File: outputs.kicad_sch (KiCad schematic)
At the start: 42 parts, among them Q1 SQ2362CES, Q3 SQ2362CES, Q6 SQ2362CES, Q7 SQ2362CES, Q8 SQ2362CES, U2 LM393

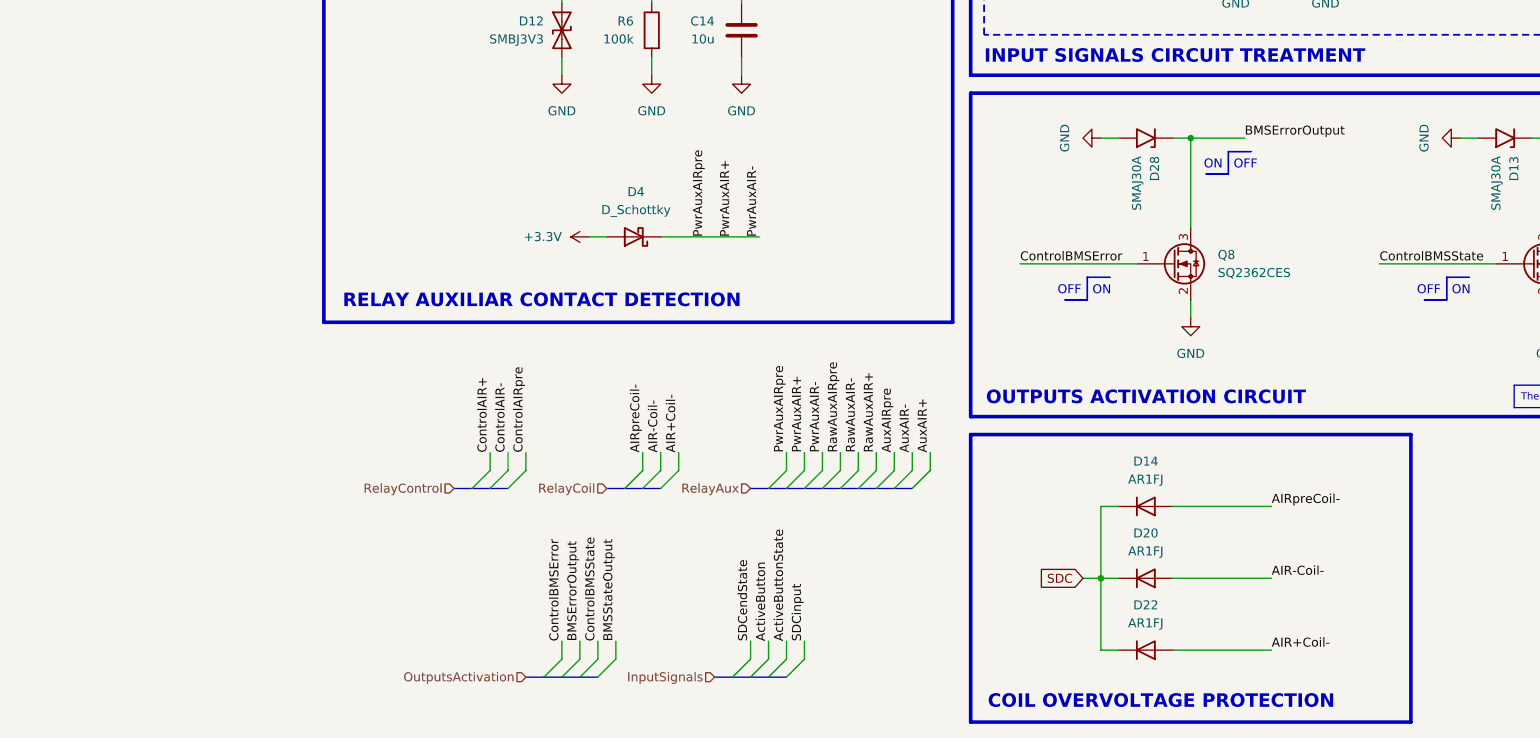
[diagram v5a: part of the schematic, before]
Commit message: - S'han afegit uns connectors preliminar \n-S'han eliminat els diodes de protecció dels airs
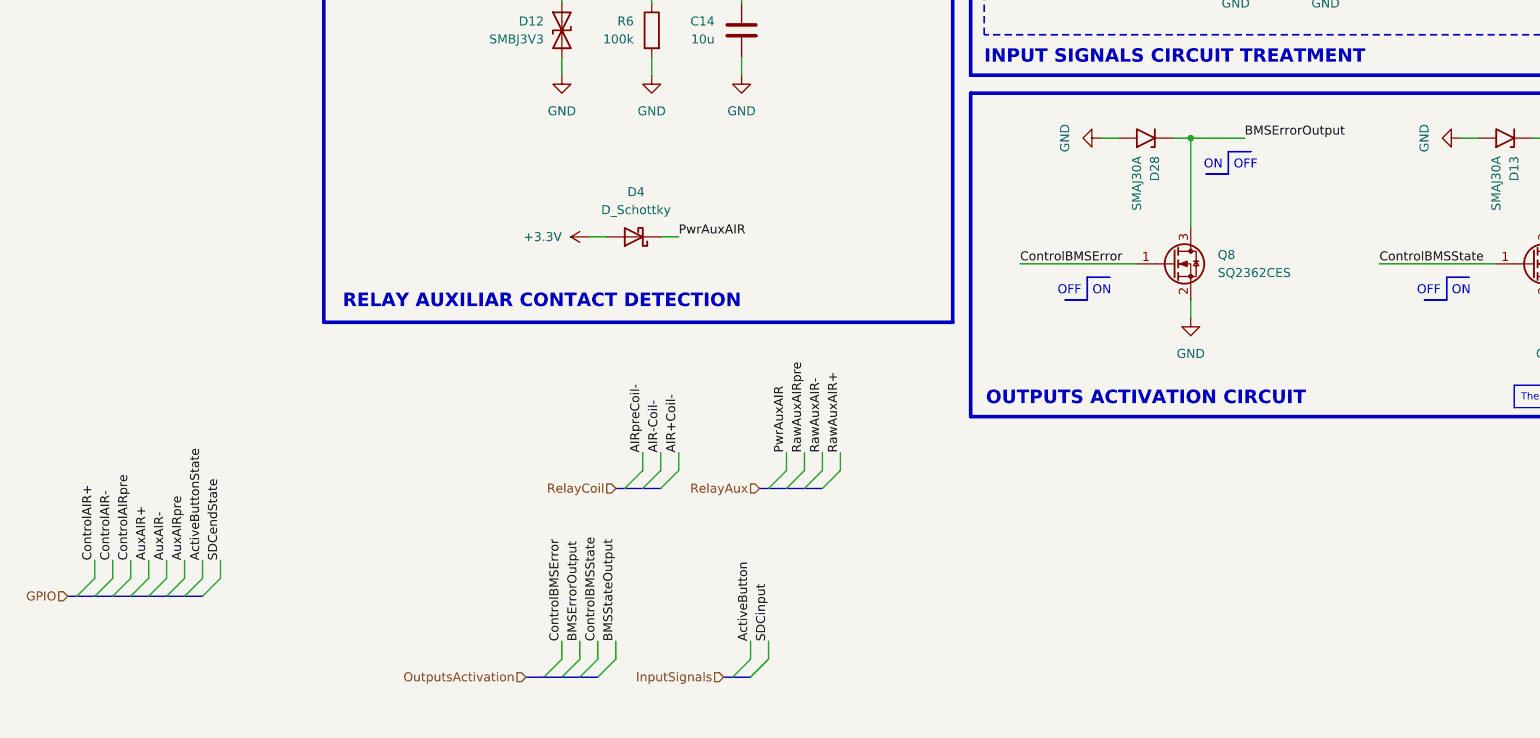
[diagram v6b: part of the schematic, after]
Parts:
- removed D14, D20, D22: AR1FJ, Diode_SMD:D_SMF, symbol Device:D
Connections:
- net PwrAuxAIR+ renamed PwrAuxAIR
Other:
- note removed: "COIL OVERVOLTAGE PROTECTION"

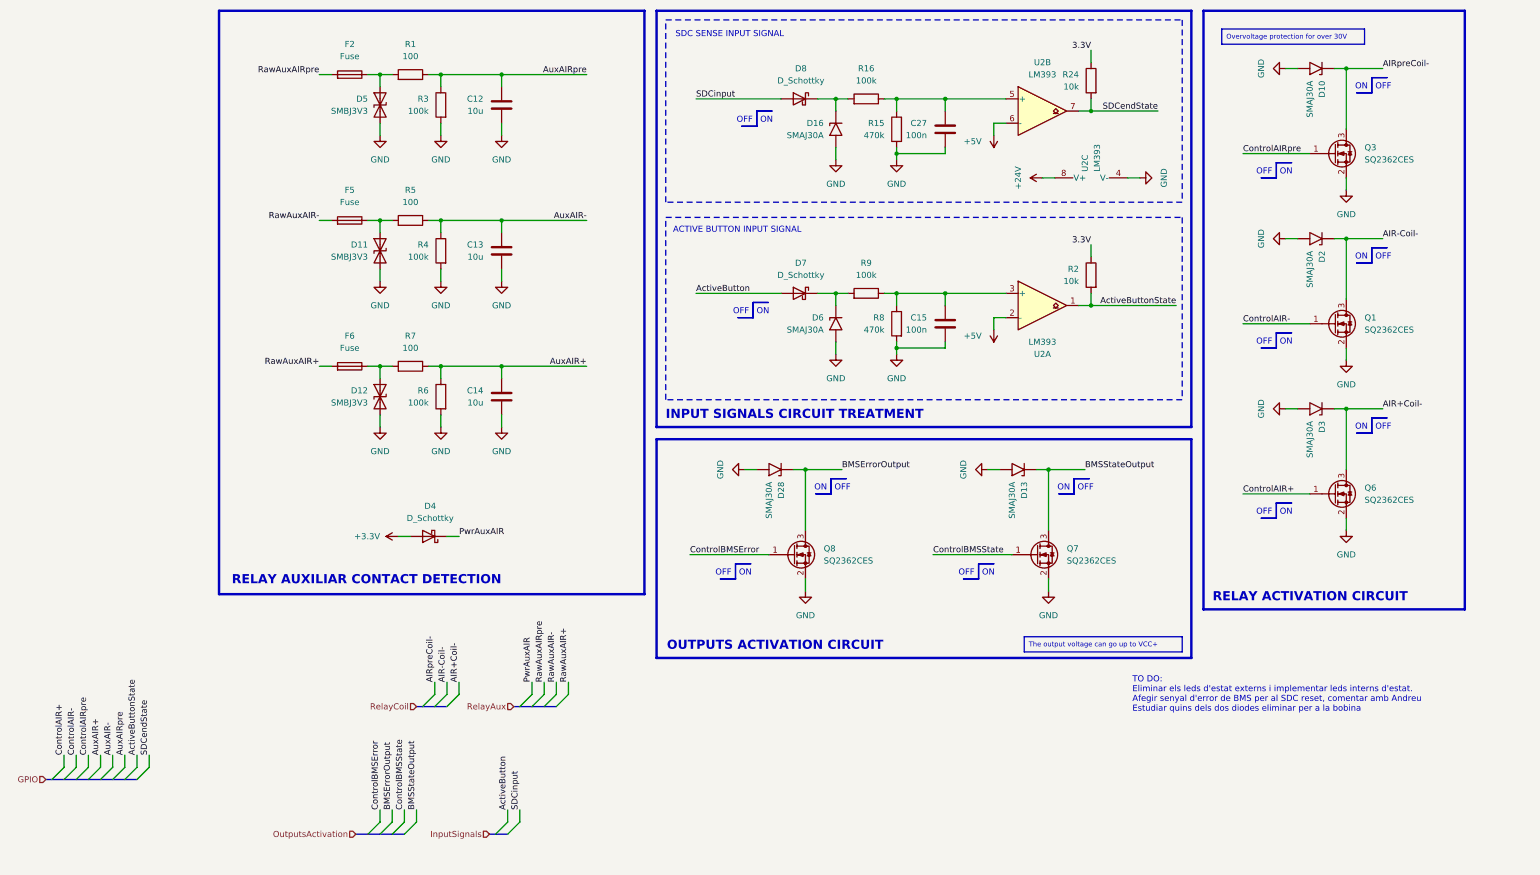
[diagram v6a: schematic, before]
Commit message: Modificació de les etiquetes a globals Filtre afegit al transformador de isoSPI Leds indicadors per estat i error Senyal d'error de BMS per el sdcreset
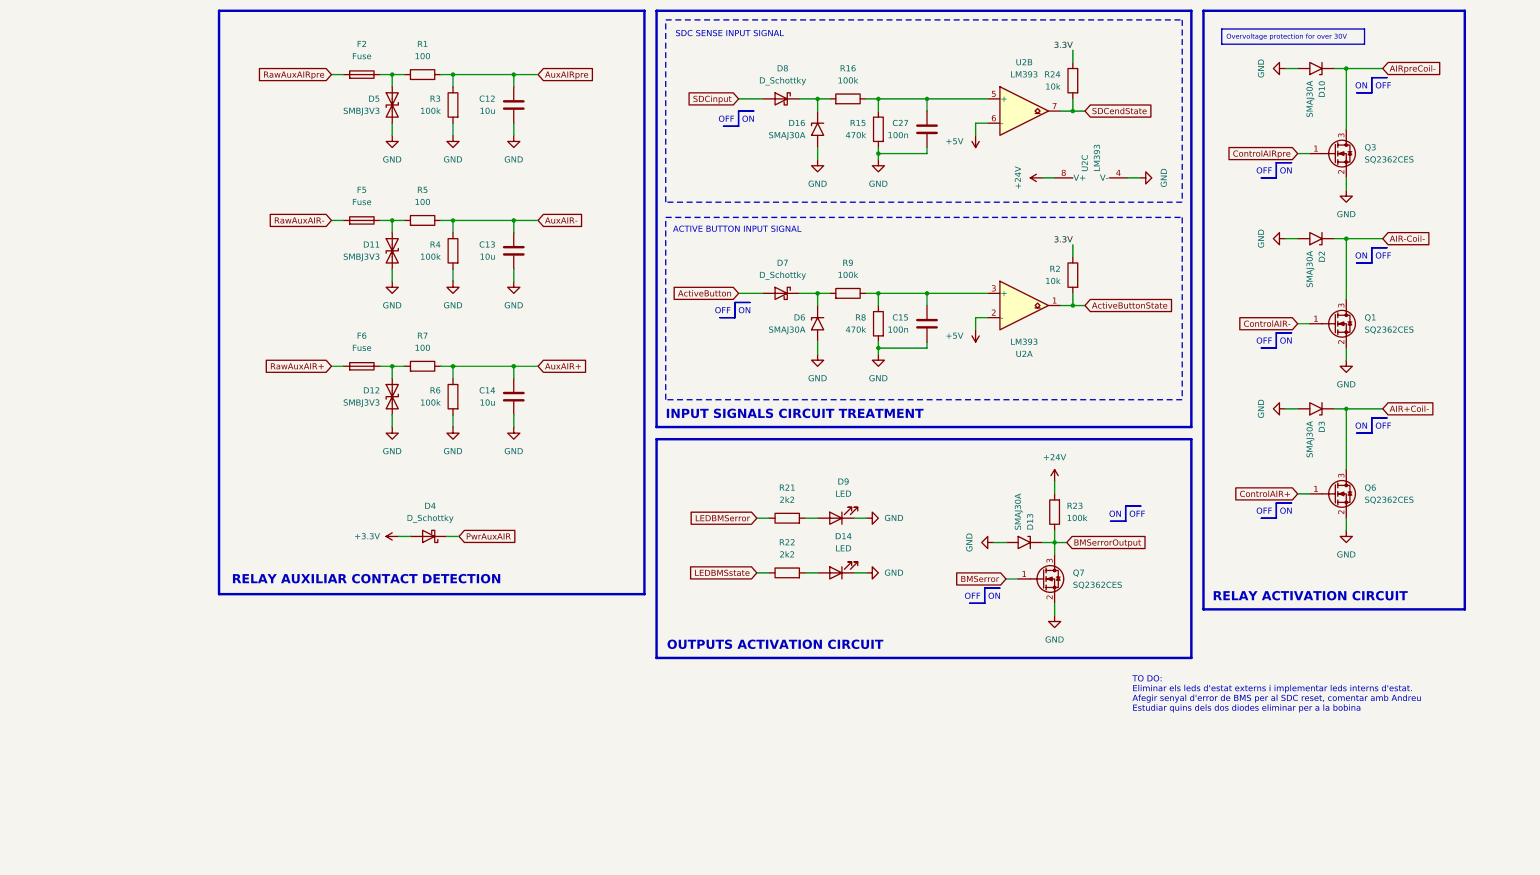
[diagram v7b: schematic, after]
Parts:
- removed D28: SMAJ30A, Diode_SMD:D_SMA, symbol Diode:SMAJ30A
- removed Q8: SQ2362CES, Package_TO_SOT_SMD:SOT-23, symbol Transistor_FET:2N7002
- added D14, D9: LED, LED_SMD:LED_0603_1608Metric_Pad1.05x0.95mm_HandSolder, symbol Device:LED
- added R21, R22: 2k2, Resistor_SMD:R_0603_1608Metric, symbol Device:R
- added R23: 100k, Resistor_SMD:R_0603_1608Metric, symbol Device:R
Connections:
- net +24V: now also R23.2
- net GND: now also D14.1 (K), D9.1 (K)
- net BMSStateOutput renamed BMSerrorOutput
- net BMSerrorOutput: now also R23.1
- net ControlBMSState renamed BMSerror
- new net: D14.2 (A), R22.2
- new net: D9.2 (A), R21.2
- new net LEDBMSerror: R21.1
- new net LEDBMSstate: R22.1
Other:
- moved on the sheet: C12, C13, C14, C15, C27, D11, D12, D13, D16, D5, D6, D7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

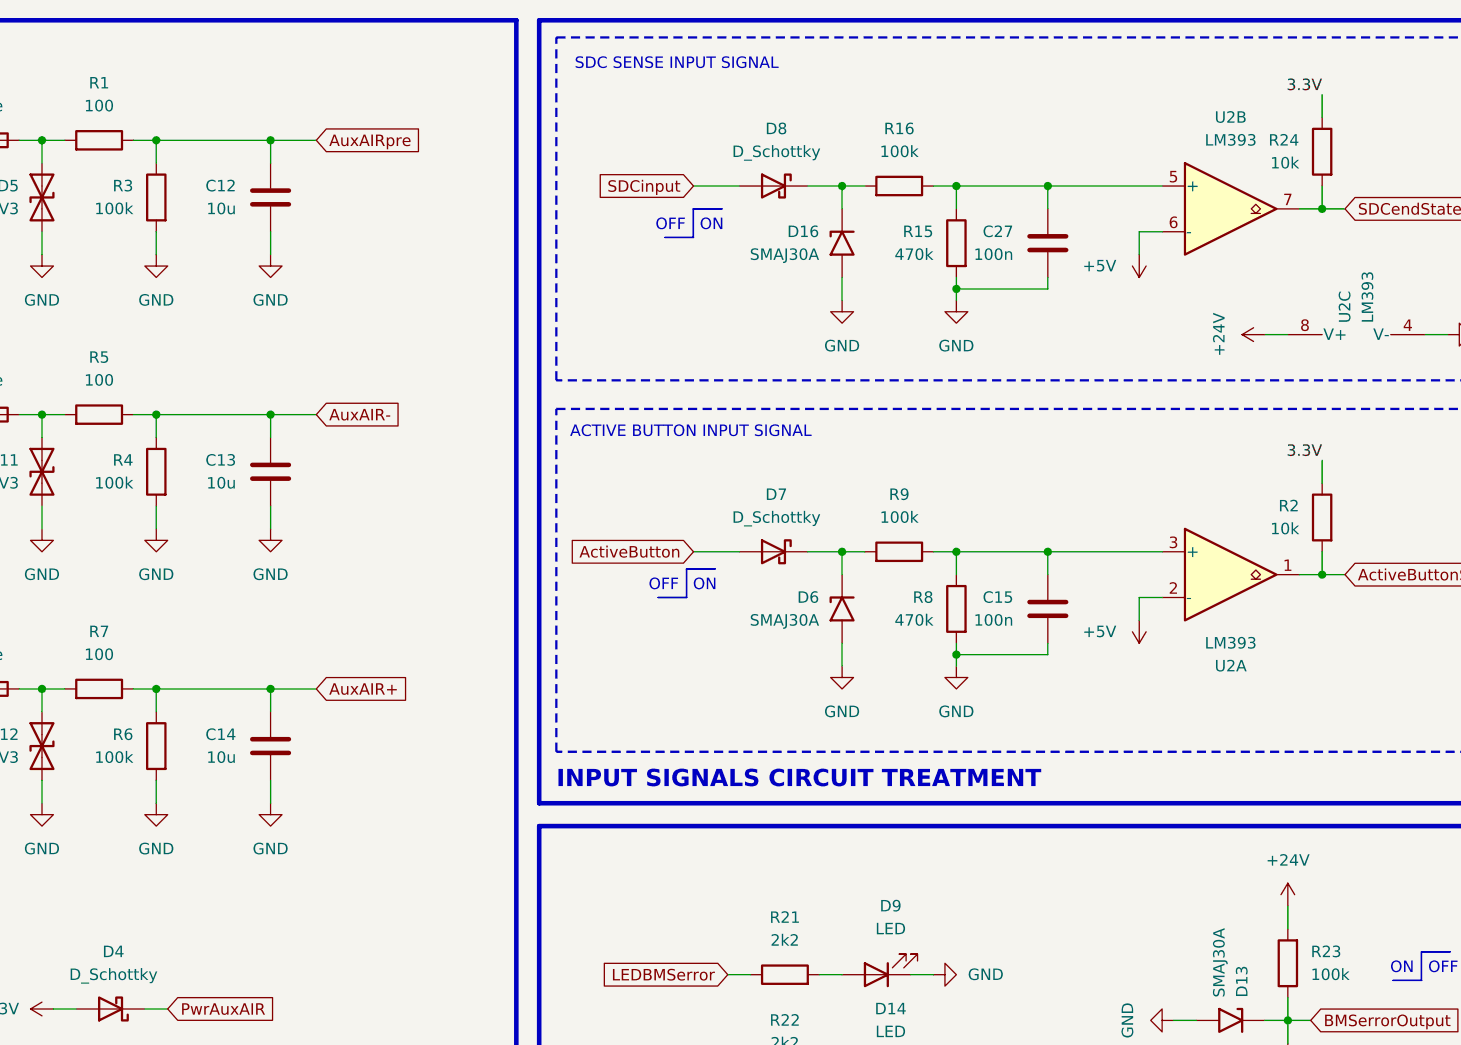
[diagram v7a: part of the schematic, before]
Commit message: Revisió dels valors de filtres, divisors de tensió i resistències
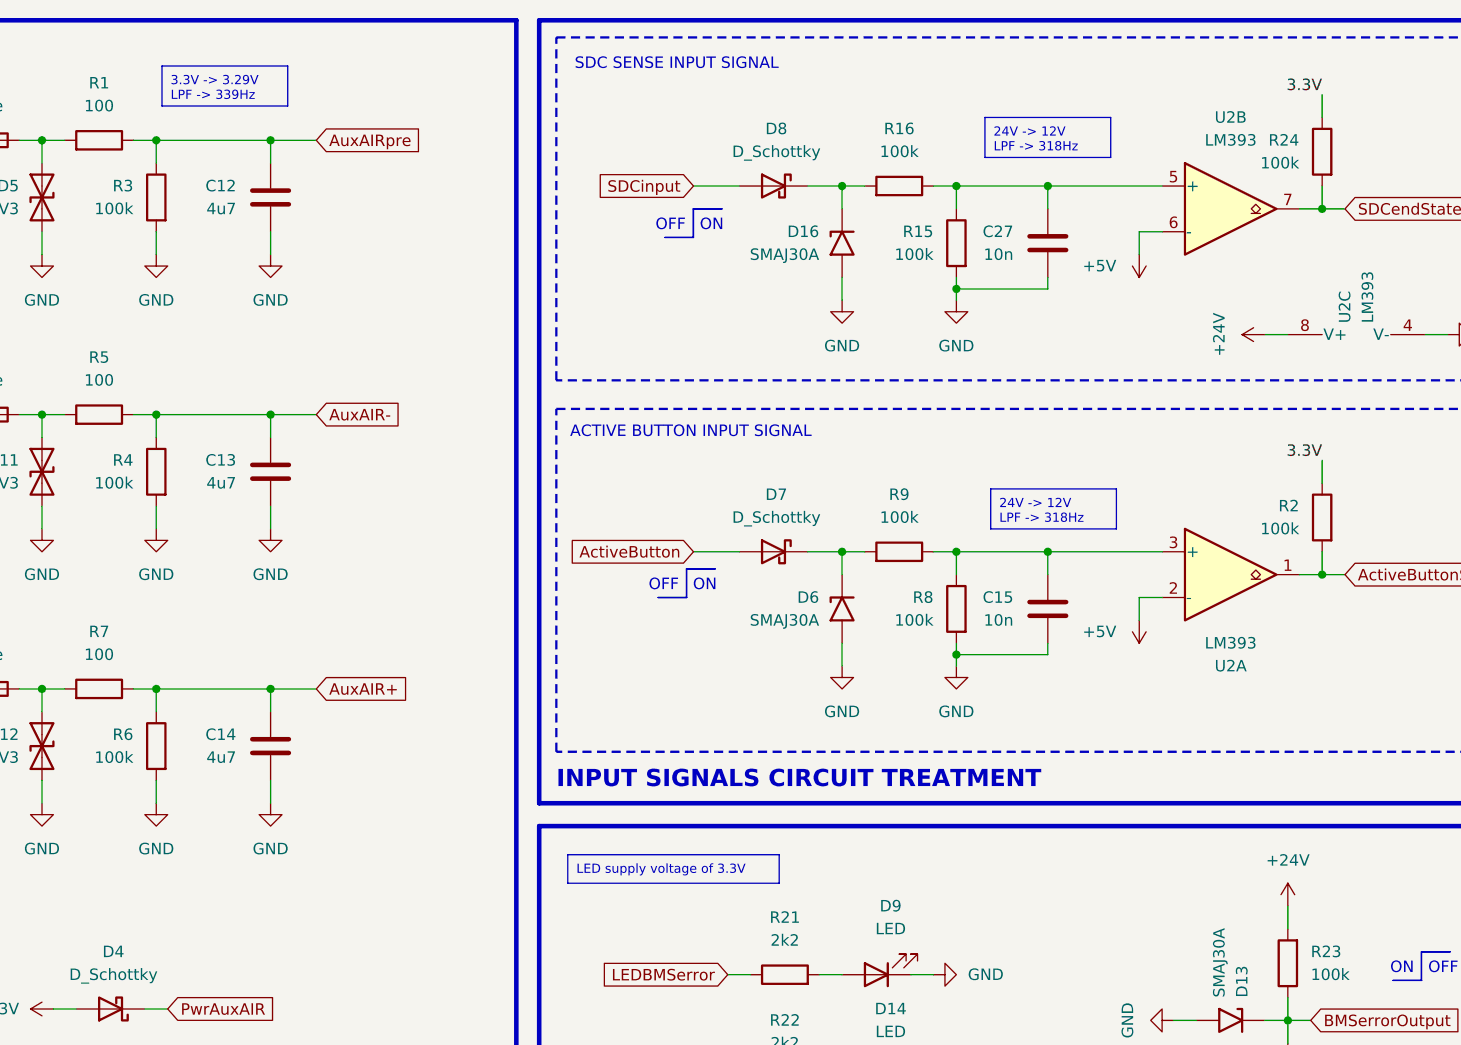
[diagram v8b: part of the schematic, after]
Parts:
- C12, C13, C14: value 10u -> 4u7
- C15, C27: value 100n -> 10n
- R15, R8: value 470k -> 100k
- R2, R24: value 10k -> 100k
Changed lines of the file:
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@@
 		)
 	)
+	(text_box "24V -> 12V\nLPF -> 318Hz"
+		(exclude_from_sim no)
+		(at 162.56 69.215 0)
+		(size 13.97 4.445)
+		(margins 0.9525 0.9525 0.9525 0.9525)
+		(stroke
+			(width 0)
+			(type solid)
+			(color 132 0 0 1)
+		)
+		(fill
+			(type color)
+			(color 255 255 194 1)
+		)
+		(effects
+			(font
+				(size 1.016 1.016)
+				(color 0 0 0 1)
+			)
+			(justify left top)
+		)
+	)
+	(text_box "24V -> 12V\nLPF -> 318Hz"
+		(exclude_from_sim no)
+		(at 161.925 27.94 0)
+		(size 13.97 4.445)
+		(margins 0.9525 0.9525 0.9525 0.9525)
+		(stroke
+			(width 0)
+			(type solid)
+			(color 132 0 0 1)
+		)
+		(fill
+			(type color)
+			(color 255 255 194 1)
+		)
+		(effects
+			(font
+				(size 1.016 1.016)
+				(color 0 0 0 1)
+			)
+			(justify left top)
+		)
+	)
+	(text_box "3.3V -> 3.29V\nLPF -> 339Hz"
+		(exclude_from_sim no)
+		(at 70.485 22.225 0)
+		(size 13.97 4.445)
+		(margins 0.9525 0.9525 0.9525 0.9525)
+		(stroke
+			(width 0)
+			(type solid)
+			(color 132 0 0 1)
+		)
+		(fill
+			(type color)
+			(color 255 255 194 1)
+		)
+		(effects
+			(font
+				(size 1.016 1.016)
+				(color 0 0 0 1)
+			)
+			(justify left top)
+		)
+	)
+	(text_box "LED supply voltage of 3.3V"
+		(exclude_from_sim no)
+		(at 115.57 109.855 0)
+		(size 23.495 3.175)
+		(margins 0.9525 0.9525 0.9525 0.9525)
+		(stroke
+			(width 0)
+			(type solid)
+			(color 132 0 0 1)
+		)
+		(fill
+			(type color)
+			(color 255 255 194 1)
+		)
+		(effects
+			(font
+				(size 1.016 1.016)
+				(color 0 0 0 1)
+			)
+			(justify left top)
+		)
+	)
 	(text_box "Overvoltage protection for over 30V"
 		(exclude_from_sim no)
@@
 			)
 		)
-		(property "Value" "100n"
+		(property "Value" "10n"
 			(at 165.1 43.1799 0)
 			(effects
@@
 			)
 		)
-		(property "Value" "10u"
+		(property "Value" "4u7"
 			(at 78.74 38.0999 0)
 			(effects
@@
 			)
 		)
-		(property "Value" "470k"
+		(property "Value" "100k"
 			(at 156.21 83.8199 0)
 			(effects
@@
 			)
 		)
-		(property "Value" "10k"
+		(property "Value" "100k"
 			(at 196.85 73.6599 0)
 			(effects
@@
 			)
 		)
-		(property "Value" "470k"
+		(property "Value" "100k"
 			(at 156.21 43.1799 0)
 			(effects
@@
 			)
 		)
-		(property "Value" "10k"
+		(property "Value" "100k"
 			(at 196.85 33.0199 0)
 			(effects
@@
 			)
 		)
-		(property "Value" "100n"
+		(property "Value" "10n"
 			(at 165.1 83.8199 0)
 			(effects
@@
 			)
 		)
-		(property "Value" "10u"
+		(property "Value" "4u7"
 			(at 78.74 68.5799 0)
 			(effects
@@
 			)
 		)
-		(property "Value" "10u"
+		(property "Value" "4u7"
 			(at 78.74 99.0599 0)
 			(effects
